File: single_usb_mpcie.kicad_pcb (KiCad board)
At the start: 2 copper layers, 35 x 85 mm, 15 parts, among them J1 91304-56-052R2, J2 USB_B_Micro, U1 AZ1117H-3.3

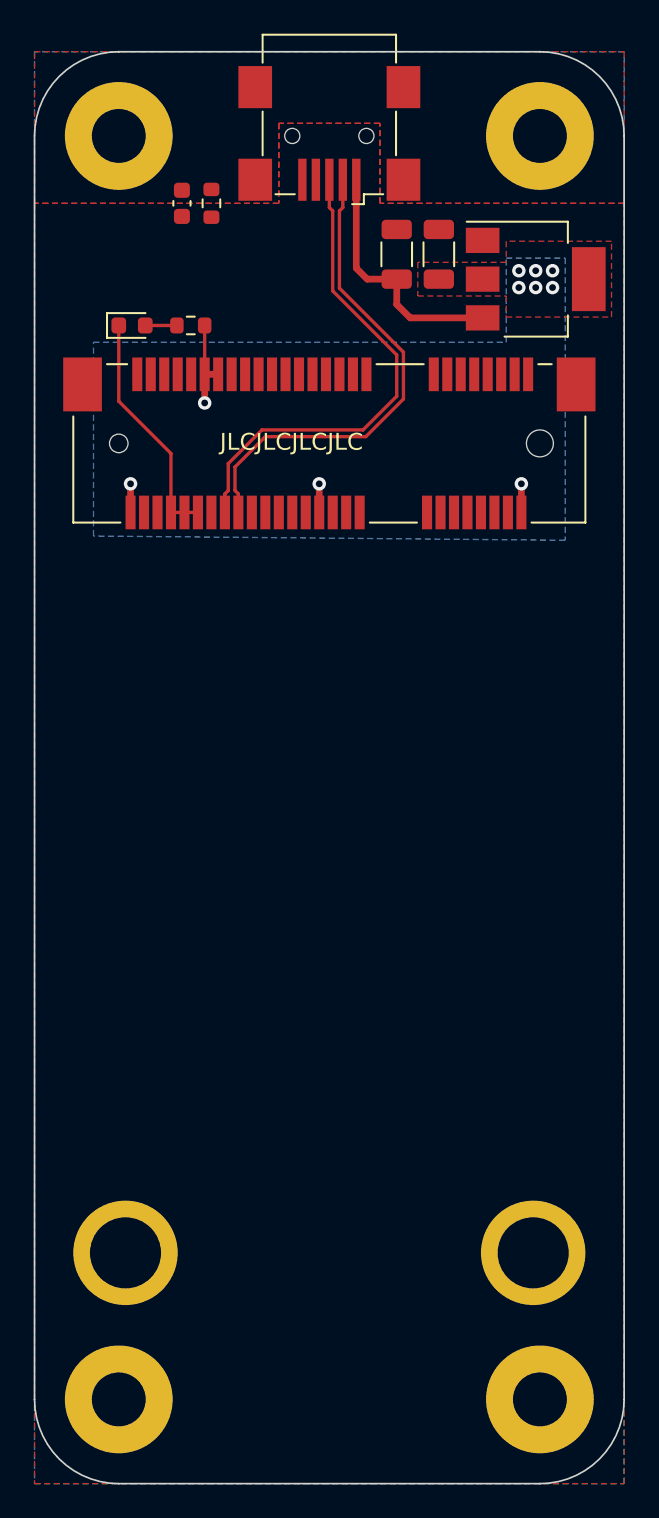
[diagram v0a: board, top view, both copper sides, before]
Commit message: Change mounting holes to #6-32
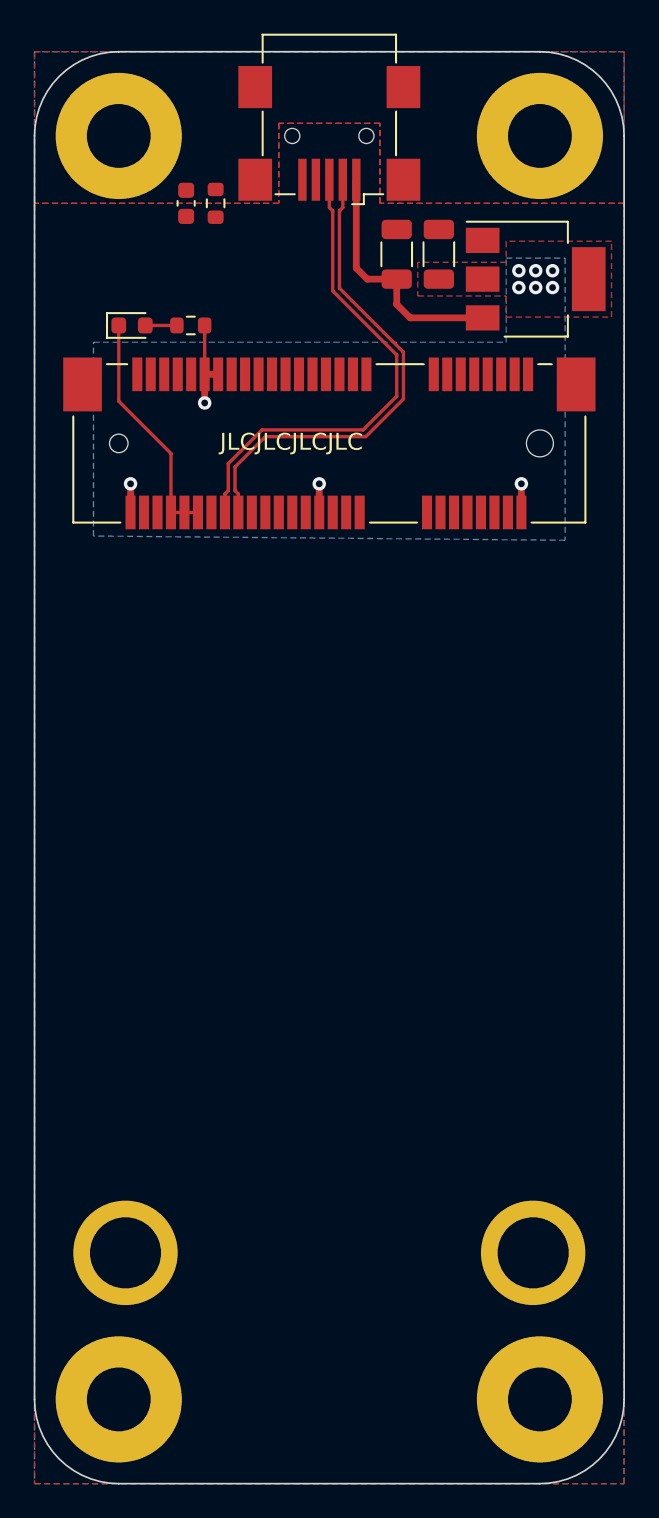
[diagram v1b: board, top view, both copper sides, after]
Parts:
- H1, H2, H3, H4: footprint MountingHole:MountingHole_3.2mm_M3_Pad -> parts:MountingHole_6-32_Pad
- moved C1 0.25 mm to (118.5, 46.8)
- moved R1 0.25 mm to (120.2, 46.8)
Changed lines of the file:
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@@
     )
   )
-  (footprint "MountingHole:MountingHole_3.2mm_M3_Pad" (layer "F.Cu")
+  (footprint "parts:MountingHole_6-32_Pad" (layer "F.Cu")
     (at 114.5 117.75)
-    (descr "Mounting Hole 3.2mm, M3")
-    (tags "mounting hole 3.2mm m3")
-    (property "LCSC" "")
-    (property "Sheetfile" "single_usb_mpcie.kicad_sch")
-    (property "Sheetname" "")
-    (property "ki_description" "Mounting Hole with connection")
-    (property "ki_keywords" "mounting hole")
-    (attr exclude_from_pos_files)
-    (fp_text reference "H1" (at 0 -4.2) (layer "Cmts.User")
-        (effects (font (size 1 1) (thickness 0.15)))
-    )
-    (fp_text value "M3" (at 0 4.2) (layer "F.Fab")
-        (effects (font (size 1 1) (thickness 0.15)))
-    )
-    (fp_text user "${REFERENCE}" (at 0 0) (layer "F.Fab")
-        (effects (font (size 1 1) (thickness 0.15)))
-    )
-    (fp_circle (center 0 0) (end 3.2 0)
-      (stroke (width 0.15) (type solid)) (fill none) (layer "Cmts.User"))
-    (fp_circle (center 0 0) (end 3.45 0)
-      (stroke (width 0.05) (type solid)) (fill none) (layer "F.CrtYd"))
-    (pad "1" thru_hole circle (at 0 0) (size 6.4 6.4) (drill 3.2) (layers "*.Cu" "*.Mask")
-      (net 1 "/SHIELD") (pinfunction "1") (pintype "input"))
-  )
-  (footprint "MountingHole:MountingHole_3.2mm_M3_Pad" (layer "F.Cu")
+    (descr "Mounting Hole 6-32")
+    (tags "mounting hole 6-32")
+    (property "LCSC" "")
+    (property "Sheetfile" "single_usb_mpcie.kicad_sch")
+    (property "Sheetname" "")
+    (property "ki_description" "Mounting Hole with connection")
+    (property "ki_keywords" "mounting hole")
+    (attr exclude_from_pos_files)
+    (fp_text reference "H1" (at 0 -4.7) (layer "Cmts.User")
+        (effects (font (size 1 1) (thickness 0.15)))
+    )
+    (fp_text value "M3" (at 0 4.7) (layer "F.Fab")
+        (effects (font (size 1 1) (thickness 0.15)))
+    )
+    (fp_text user "${REFERENCE}" (at 0 0) (layer "F.Fab")
+        (effects (font (size 1 1) (thickness 0.15)))
+    )
+    (fp_circle (center 0 0) (end 3.79 0)
+      (stroke (width 0.15) (type solid)) (fill none) (layer "Cmts.User"))
+    (fp_circle (center 0 0) (end 3.95 0)
+      (stroke (width 0.05) (type solid)) (fill none) (layer "F.CrtYd"))
+    (pad "1" thru_hole circle (at 0 0) (size 7.49 7.49) (drill 3.79) (layers "*.Cu" "*.Mask")
+      (net 1 "/SHIELD") (pinfunction "1") (pintype "input"))
+  )
+  (footprint "parts:MountingHole_6-32_Pad" (layer "F.Cu")
     (at 114.5 42.75)
-    (descr "Mounting Hole 3.2mm, M3")
-    (tags "mounting hole 3.2mm m3")
-    (property "LCSC" "")
-    (property "Sheetfile" "single_usb_mpcie.kicad_sch")
-    (property "Sheetname" "")
-    (property "ki_description" "Mounting Hole with connection")
-    (property "ki_keywords" "mounting hole")
-    (attr exclude_from_pos_files)
-    (fp_text reference "H4" (at 0 -4.2) (layer "Cmts.User")
-        (effects (font (size 1 1) (thickness 0.15)))
-    )
-    (fp_text value "M3" (at 0 4.2) (layer "F.Fab")
-        (effects (font (size 1 1) (thickness 0.15)))
-    )
-    (fp_text user "${REFERENCE}" (at 0 0) (layer "F.Fab")
-        (effects (font (size 1 1) (thickness 0.15)))
-    )
-    (fp_circle (center 0 0) (end 3.2 0)
-      (stroke (width 0.15) (type solid)) (fill none) (layer "Cmts.User"))
-    (fp_circle (center 0 0) (end 3.45 0)
-      (stroke (width 0.05) (type solid)) (fill none) (layer "F.CrtYd"))
-    (pad "1" thru_hole circle (at 0 0) (size 6.4 6.4) (drill 3.2) (layers "*.Cu" "*.Mask")
+    (descr "Mounting Hole 6-32")
+    (tags "mounting hole 6-32")
+    (property "LCSC" "")
+    (property "Sheetfile" "single_usb_mpcie.kicad_sch")
+    (property "Sheetname" "")
+    (property "ki_description" "Mounting Hole with connection")
+    (property "ki_keywords" "mounting hole")
+    (attr exclude_from_pos_files)
+    (fp_text reference "H4" (at 0 -4.7) (layer "Cmts.User")
+        (effects (font (size 1 1) (thickness 0.15)))
+    )
+    (fp_text value "M3" (at 0 4.7) (layer "F.Fab")
+        (effects (font (size 1 1) (thickness 0.15)))
+    )
+    (fp_text user "${REFERENCE}" (at 0 0) (layer "F.Fab")
+        (effects (font (size 1 1) (thickness 0.15)))
+    )
+    (fp_circle (center 0 0) (end 3.79 0)
+      (stroke (width 0.15) (type solid)) (fill none) (layer "Cmts.User"))
+    (fp_circle (center 0 0) (end 3.95 0)
+      (stroke (width 0.05) (type solid)) (fill none) (layer "F.CrtYd"))
+    (pad "1" thru_hole circle (at 0 0) (size 7.49 7.49) (drill 3.79) (layers "*.Cu" "*.Mask")
       (net 1 "/SHIELD") (pinfunction "1") (pintype "input"))
   )
   (footprint "Resistor_SMD:R_0603_1608Metric" (layer "F.Cu")
-    (at 120 46.75 -90)
+    (at 120.25 46.75 -90)
     (descr "Resistor SMD 0603 (1608 Metric), square (rectangular) end terminal, IPC_7351 nominal, (Body size source: IPC-SM-782 page 72, https://www.pcb-3d.com/wordpress/wp-content/uploads/ipc-sm-782a_amendment_1_and_2.pdf), generated with kicad-footprint-generator")
     (tags "resistor")
@@
     )
   )
-  (footprint "MountingHole:MountingHole_3.2mm_M3_Pad" (layer "F.Cu")
+  (footprint "parts:MountingHole_6-32_Pad" (layer "F.Cu")
     (at 139.5 117.75)
-    (descr "Mounting Hole 3.2mm, M3")
-    (tags "mounting hole 3.2mm m3")
-    (property "LCSC" "")
-    (property "Sheetfile" "single_usb_mpcie.kicad_sch")
-    (property "Sheetname" "")
-    (property "ki_description" "Mounting Hole with connection")
-    (property "ki_keywords" "mounting hole")
-    (attr exclude_from_pos_files)
-    (fp_text reference "H2" (at 0 -4.2) (layer "Cmts.User")
-        (effects (font (size 1 1) (thickness 0.15)))
-    )
-    (fp_text value "M3" (at 0 4.2) (layer "F.Fab")
-        (effects (font (size 1 1) (thickness 0.15)))
-    )
-    (fp_text user "${REFERENCE}" (at 0 0) (layer "F.Fab")
-        (effects (font (size 1 1) (thickness 0.15)))
-    )
-    (fp_circle (center 0 0) (end 3.2 0)
-      (stroke (width 0.15) (type solid)) (fill none) (layer "Cmts.User"))
-    (fp_circle (center 0 0) (end 3.45 0)
-      (stroke (width 0.05) (type solid)) (fill none) (layer "F.CrtYd"))
-    (pad "1" thru_hole circle (at 0 0) (size 6.4 6.4) (drill 3.2) (layers "*.Cu" "*.Mask")
-      (net 1 "/SHIELD") (pinfunction "1") (pintype "input"))
-  )
-  (footprint "MountingHole:MountingHole_3.2mm_M3_Pad" (layer "F.Cu")
+    (descr "Mounting Hole 6-32")
+    (tags "mounting hole 6-32")
+    (property "LCSC" "")
+    (property "Sheetfile" "single_usb_mpcie.kicad_sch")
+    (property "Sheetname" "")
+    (property "ki_description" "Mounting Hole with connection")
+    (property "ki_keywords" "mounting hole")
+    (attr exclude_from_pos_files)
+    (fp_text reference "H2" (at 0 -4.7) (layer "Cmts.User")
+        (effects (font (size 1 1) (thickness 0.15)))
+    )
+    (fp_text value "M3" (at 0 4.7) (layer "F.Fab")
+        (effects (font (size 1 1) (thickness 0.15)))
+    )
+    (fp_text user "${REFERENCE}" (at 0 0) (layer "F.Fab")
+        (effects (font (size 1 1) (thickness 0.15)))
+    )
+    (fp_circle (center 0 0) (end 3.79 0)
+      (stroke (width 0.15) (type solid)) (fill none) (layer "Cmts.User"))
+    (fp_circle (center 0 0) (end 3.95 0)
+      (stroke (width 0.05) (type solid)) (fill none) (layer "F.CrtYd"))
+    (pad "1" thru_hole circle (at 0 0) (size 7.49 7.49) (drill 3.79) (layers "*.Cu" "*.Mask")
+      (net 1 "/SHIELD") (pinfunction "1") (pintype "input"))
+  )
+  (footprint "parts:MountingHole_6-32_Pad" (layer "F.Cu")
     (at 139.5 42.75)
-    (descr "Mounting Hole 3.2mm, M3")
-    (tags "mounting hole 3.2mm m3")
-    (property "LCSC" "")
-    (property "Sheetfile" "single_usb_mpcie.kicad_sch")
-    (property "Sheetname" "")
-    (property "ki_description" "Mounting Hole with connection")
-    (property "ki_keywords" "mounting hole")
-    (attr exclude_from_pos_files)
-    (fp_text reference "H3" (at 0 -4.2) (layer "Cmts.User")
-        (effects (font (size 1 1) (thickness 0.15)))
-    )
-    (fp_text value "M3" (at 0 4.2) (layer "F.Fab")
-        (effects (font (size 1 1) (thickness 0.15)))
-    )
-    (fp_text user "${REFERENCE}" (at 0 0) (layer "F.Fab")
-        (effects (font (size 1 1) (thickness 0.15)))
-    )
-    (fp_circle (center 0 0) (end 3.2 0)
-      (stroke (width 0.15) (type solid)) (fill none) (layer "Cmts.User"))
-    (fp_circle (center 0 0) (end 3.45 0)
-      (stroke (width 0.05) (type solid)) (fill none) (layer "F.CrtYd"))
-    (pad "1" thru_hole circle (at 0 0) (size 6.4 6.4) (drill 3.2) (layers "*.Cu" "*.Mask")
+    (descr "Mounting Hole 6-32")
+    (tags "mounting hole 6-32")
+    (property "LCSC" "")
+    (property "Sheetfile" "single_usb_mpcie.kicad_sch")
+    (property "Sheetname" "")
+    (property "ki_description" "Mounting Hole with connection")
+    (property "ki_keywords" "mounting hole")
+    (attr exclude_from_pos_files)
+    (fp_text reference "H3" (at 0 -4.7) (layer "Cmts.User")
+        (effects (font (size 1 1) (thickness 0.15)))
+    )
+    (fp_text value "M3" (at 0 4.7) (layer "F.Fab")
+        (effects (font (size 1 1) (thickness 0.15)))
+    )
+    (fp_text user "${REFERENCE}" (at 0 0) (layer "F.Fab")
+        (effects (font (size 1 1) (thickness 0.15)))
+    )
+    (fp_circle (center 0 0) (end 3.79 0)
+      (stroke (width 0.15) (type solid)) (fill none) (layer "Cmts.User"))
+    (fp_circle (center 0 0) (end 3.95 0)
+      (stroke (width 0.05) (type solid)) (fill none) (layer "F.CrtYd"))
+    (pad "1" thru_hole circle (at 0 0) (size 7.49 7.49) (drill 3.79) (layers "*.Cu" "*.Mask")
       (net 1 "/SHIELD") (pinfunction "1") (pintype "input"))
   )
@@
   )
   (footprint "Capacitor_SMD:C_0603_1608Metric" (layer "F.Cu")
-    (at 118.25 46.75 -90)
+    (at 118.5 46.75 -90)
     (descr "Capacitor SMD 0603 (1608 Metric), square (rectangular) end terminal, IPC_7351 nominal, (Body size source: IPC-SM-782 page 76, https://www.pcb-3d.com/wordpress/wp-content/uploads/ipc-sm-782a_amendment_1_and_2.pdf), generated with kicad-footprint-generator")
     (tags "capacitor")

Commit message: Add ESD on USB lines. Add noise filtering to VBUS. Change to a 4-layer board with ground / power planes.
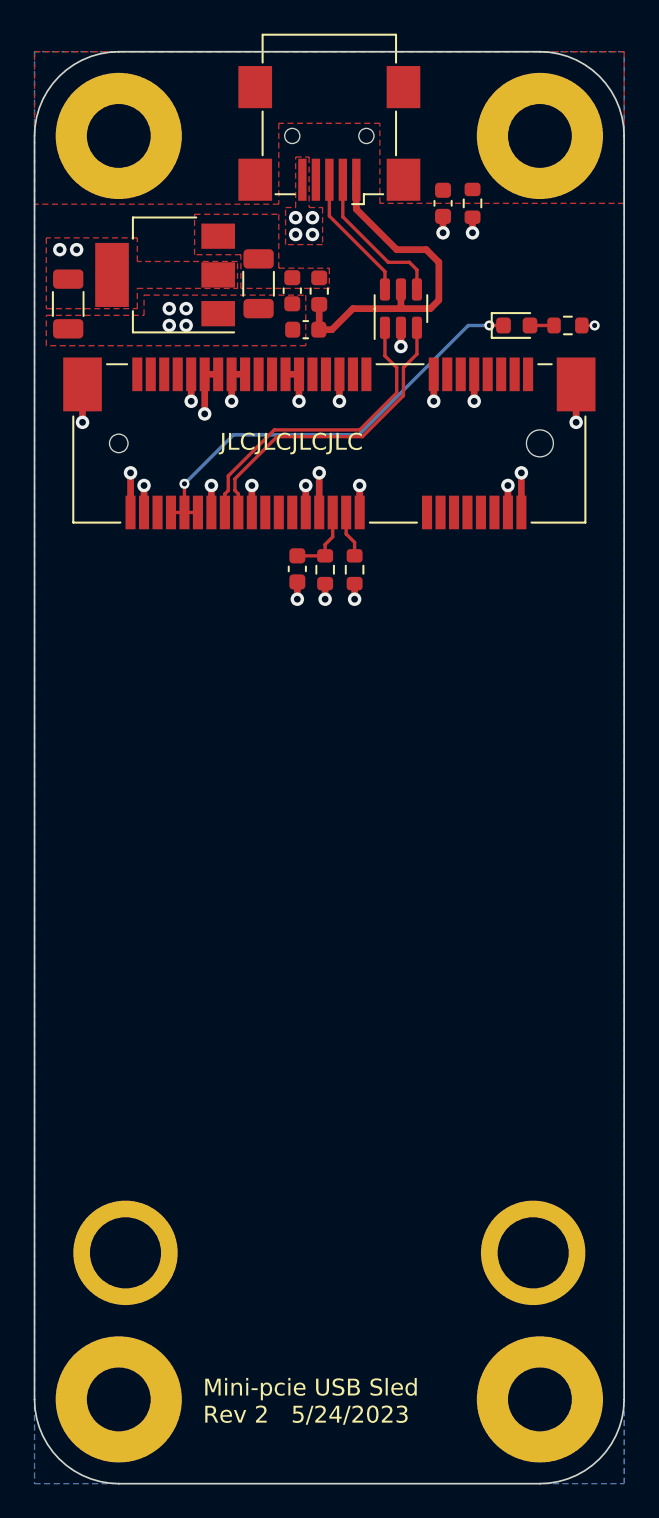
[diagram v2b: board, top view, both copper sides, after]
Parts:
- added C4: 0.1uF, Capacitor_SMD:C_0603_1608Metric, F.Cu at (125.1, 68.5)
- added C5: 0.01uF, Capacitor_SMD:C_0603_1608Metric, F.Cu at (125.6, 54.2)
- added C6: 0.01uF, Capacitor_SMD:C_0603_1608Metric, F.Cu at (124.8, 51.9)
- added FB1: ferrite_600, Inductor_SMD:L_0603_1608Metric, F.Cu at (126.4, 52.0)
- added R3: 3.3k, Resistor_SMD:R_0603_1608Metric, F.Cu at (128.5, 68.5)
- added R4: 3.3k, Resistor_SMD:R_0603_1608Metric, F.Cu at (126.8, 68.5)
- added U2: USBLC6-2SC6, Package_TO_SOT_SMD:SOT-23-6, F.Cu at (131.2, 53.0)
- H1, H2, H3, H4: value M3 -> #6-32
- moved D1 22.8 mm to (138.1, 54.0)
- moved R2 22.4 mm to (141.2, 54.0)
- moved C3 22.2 mm to (111.5, 52.7), turned to -90 degrees
- moved U1 22.0 mm to (117.2, 51.0), turned to 180 degrees
- moved C1 15.2 mm to (133.8, 46.8)
- moved R1 15.2 mm to (135.5, 46.8)
- moved C2 8.38 mm to (122.8, 51.5), turned to -90 degrees
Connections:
- J1 pad 20: unconnected-(J1-~{W_DISABLE}-Pad20) -> Net-(J1-~{W_DISABLE})
- J1 pad 22: unconnected-(J1-~{PERST}-Pad22) -> Net-(J1-~{PERST})
- J1 pad 36: /USB- -> /USB_D-
- J1 pad 38: /USB+ -> /USB_D+
- J2 pad 1: +5V -> /VBUS
- J2 pad 2: /USB- -> /USB_C-
- J2 pad 3: /USB+ -> /USB_C+
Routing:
- net GND: track 0.00 -> 29.3 mm, vias 0 -> 26
- net /USB+: track 29.1 -> 0.00 mm
- net /USB-: track 29.1 -> 0.00 mm
- net /VBUS: track 0.00 -> 20.7 mm
- net /USB_D-: track 0.00 -> 18.5 mm
- net /USB_D+: track 0.00 -> 18.4 mm
- net +5V: track 14.9 -> 0.00 mm
- net Net-(D1-K): track 14.0 -> 26.1 mm, vias 0 -> 2
- net /USB_C-: track 0.00 -> 9.07 mm
- net /USB_C+: track 0.00 -> 7.88 mm
- net Net-(J1-~{PERST}): track 0.00 -> 4.41 mm
- net Net-(J1-~{W_DISABLE}): track 0.00 -> 2.78 mm
- net +3.3V: track 10.5 -> 12.8 mm, vias 10 -> 9
- added copper zone on In2.Cu, net +3.3V
- added copper zone on F.Cu, net +5V
- added copper zone on In1.Cu, net GND
- removed copper zone on B.Cu, net +3.3V
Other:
- copper layers 2 -> 4
- board text added: "Mini-pcie USB Sled Rev 2 5/24/2023"

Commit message: Rev silkscreen. Tweak grounds
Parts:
- moved U2 2.30 mm to (129.5, 51.5)
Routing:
- net /VBUS: track 20.7 -> 17.2 mm
- net /USB_C-: track 9.07 -> 6.11 mm
- net GND: track 29.3 -> 32.2 mm, vias 26 -> 24
- net /USB_D+: track 18.4 -> 20.9 mm
- net /USB_D-: track 18.5 -> 20.7 mm
- net /USB_C+: track 7.88 -> 6.03 mm
